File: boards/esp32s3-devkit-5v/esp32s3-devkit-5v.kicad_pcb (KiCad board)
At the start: 4 copper layers, 59.3 x 38 mm, 37 parts, among them J1 Conn_01x17_Pin, J2 Conn_01x17_Pin, J3 USB_C_Receptacle_USB2.0_16P, Q1 AO3401A, SW1 MK-12C03-G015, SW2 RESET, SW3 BOOT, U1 TPS63070RNMR, U2 ESP32-S3-WROOM-1-N16, U3 USBLC6-2SC6

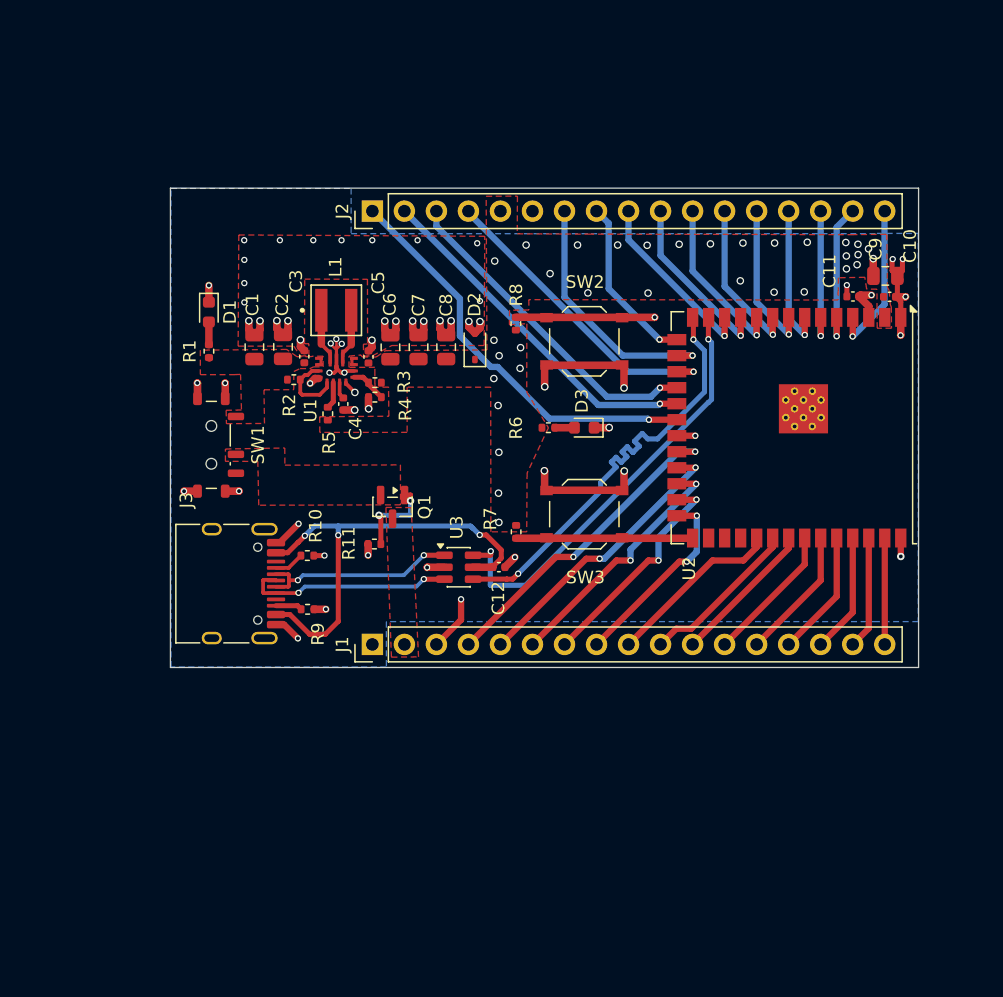
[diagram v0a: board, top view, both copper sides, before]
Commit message: feat(esp32s3-devkit-5v): add reviewed schematic and routed prototype
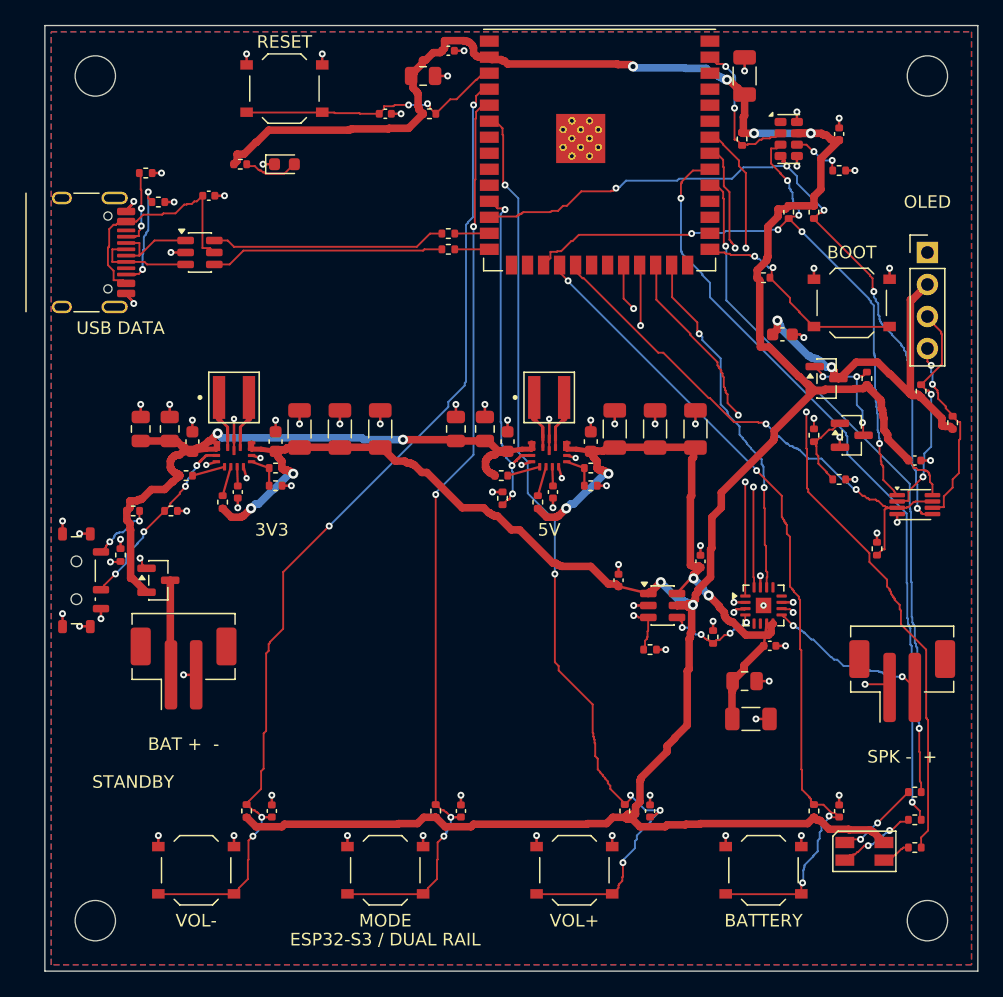
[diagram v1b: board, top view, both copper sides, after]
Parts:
- removed D3: LED, LED_SMD:LED_0603_1608Metric
- removed R2: 10kΩ, Resistor_SMD:R_0402_1005Metric
- added C13: 10µF, Capacitor_SMD:C_0603_1608Metric, F.Cu at (143.3, 103.0)
- added C14: 22µF, Capacitor_SMD:C_1206_3216Metric, F.Cu at (145.2, 102.0)
- added C15: 22µF, Capacitor_SMD:C_1206_3216Metric, F.Cu at (148.4, 102.0)
- added C16: 22µF, Capacitor_SMD:C_1206_3216Metric, F.Cu at (151.6, 102.0)
- added C17: 22µF, Capacitor_SMD:C_0805_2012Metric, F.Cu at (130.0, 74.0)
- added C18: 0.1µF, Capacitor_SMD:C_0402_1005Metric, F.Cu at (132.0, 72.0)
- added C19: 1µF, Capacitor_SMD:C_0402_1005Metric, F.Cu at (127.0, 77.0)
- added C20: 0.1µF, Capacitor_SMD:C_0402_1005Metric, F.Cu at (113.0, 83.5)
- added C21: 100µF, Capacitor_SMD:C_1206_3216Metric, F.Cu at (155.5, 74.0)
- added C22: 0.1µF, Capacitor_SMD:C_0402_1005Metric, F.Cu at (118.0, 132.3)
- added C23: 0.1µF, Capacitor_SMD:C_0402_1005Metric, F.Cu at (133.0, 132.3)
- added C24: 0.1µF, Capacitor_SMD:C_0402_1005Metric, F.Cu at (148.0, 132.3)
- added C25: 0.1µF, Capacitor_SMD:C_0402_1005Metric, F.Cu at (163.0, 132.3)
- added C26: 100µF, Capacitor_SMD:C_1206_3216Metric, F.Cu at (156.0, 125.0)
- added C27: 10µF, Capacitor_SMD:C_0805_2012Metric, F.Cu at (155.5, 122.0)
- added C28: 0.1µF, Capacitor_SMD:C_0402_1005Metric, F.Cu at (157.5, 119.2)
- added C29: 0.1µF, Capacitor_SMD:C_0402_1005Metric, F.Cu at (163.0, 78.6)
- added C30: 0.1µF, Capacitor_SMD:C_0402_1005Metric, F.Cu at (169.0, 104.5)
- added C31: 1µF, Capacitor_SMD:C_0603_1608Metric, F.Cu at (158.5, 94.5)
- added C32: 0.1µF, Capacitor_SMD:C_0402_1005Metric, F.Cu at (145.5, 114.0)
- added C33: 0.1µF, Capacitor_SMD:C_0402_1005Metric, F.Cu at (152.0, 112.5)
- added H1: M3, MountingHole_3.2mm_M3, F.Cu at (104.0, 74.0)
- added H2: M3, MountingHole_3.2mm_M3, F.Cu at (170.0, 74.0)
- added H3: M3, MountingHole_3.2mm_M3, F.Cu at (104.0, 141.0)
- added H4: M3, MountingHole_3.2mm_M3, F.Cu at (170.0, 141.0)
- added J4: Conn_01x04_Pin, Connector_PinHeader_2.54mm:PinHeader_1x04_P2.54mm_Vertical, F.Cu at (170.0, 88.0)
- added L2: 1.5µH, TPS63070:IND_XFL4020-152MEC, F.Cu at (140.0, 99.5)
- added Q2: AO3401A, Package_TO_SOT_SMD:SOT-23, F.Cu at (162.0, 98.0)
- added Q3: MMBT3904, Package_TO_SOT_SMD:SOT-23, F.Cu at (164.0, 102.5)
- added R12: 10kΩ, Resistor_SMD:R_0402_1005Metric, F.Cu at (157.0, 90.0)
- added R13: 10kΩ, Resistor_SMD:R_0402_1005Metric, F.Cu at (130.5, 77.0)
- added R14: 5.1kΩ, Resistor_SMD:R_0402_1005Metric, F.Cu at (109.0, 84.0)
- added R15: 5.1kΩ, Resistor_SMD:R_0402_1005Metric, F.Cu at (108.0, 81.7)
- added R16: 4.7kΩ, Resistor_SMD:R_0402_1005Metric, F.Cu at (159.0, 84.8)
- added R17: 4.7kΩ, Resistor_SMD:R_0402_1005Metric, F.Cu at (161.0, 84.8)
- added R18: 10kΩ, Resistor_SMD:R_0402_1005Metric, F.Cu at (155.3, 79.0)
- added R19: 100kΩ, Resistor_SMD:R_0402_1005Metric, F.Cu at (136.3, 107.5)
- added R20: 100kΩ, Resistor_SMD:R_0402_1005Metric, F.Cu at (153.0, 118.5)
- added R21: 100kΩ, Resistor_SMD:R_0402_1005Metric, F.Cu at (165.2, 98.0)
- added R22: 10kΩ, Resistor_SMD:R_0402_1005Metric, F.Cu at (161.0, 102.5)
- added R23: 100kΩ, Resistor_SMD:R_0402_1005Metric, F.Cu at (163.0, 106.0)
- added R24: 10kΩ, Resistor_SMD:R_0402_1005Metric, F.Cu at (116.0, 132.3)
- added R25: 10kΩ, Resistor_SMD:R_0402_1005Metric, F.Cu at (131.0, 132.3)
- added R26: 10kΩ, Resistor_SMD:R_0402_1005Metric, F.Cu at (146.0, 132.3)
- added R27: 10kΩ, Resistor_SMD:R_0402_1005Metric, F.Cu at (161.0, 132.3)
- added R28: 330Ω, Resistor_SMD:R_0402_1005Metric, F.Cu at (169.0, 130.8)
- added R29: 150Ω, Resistor_SMD:R_0402_1005Metric, F.Cu at (169.0, 133.0)
- added R30: 150Ω, Resistor_SMD:R_0402_1005Metric, F.Cu at (169.0, 135.2)
- added R31: 10kΩ, Resistor_SMD:R_0402_1005Metric, F.Cu at (107.0, 108.5)
- added R32: 100kΩ, Resistor_SMD:R_0402_1005Metric, F.Cu at (110.0, 108.5)
- added R33: 10kΩ, Resistor_SMD:R_0402_1005Metric, F.Cu at (163.0, 81.5)
- added R34: 22Ω, Resistor_SMD:R_0402_1005Metric, F.Cu at (132.0, 86.5)
- added R35: 22Ω, Resistor_SMD:R_0402_1005Metric, F.Cu at (132.0, 87.8)
- added R36: 100kΩ, Resistor_SMD:R_0402_1005Metric, F.Cu at (166.0, 111.5)
- added R37: 4.7kΩ, Resistor_SMD:R_0402_1005Metric, F.Cu at (169.5, 99.0)
- added R38: 4.7kΩ, Resistor_SMD:R_0402_1005Metric, F.Cu at (172.0, 101.5)
- added R39: 100kΩ, Resistor_SMD:R_0402_1005Metric, F.Cu at (148.0, 119.5)
- added SW4: VOL-, Button_Switch_SMD:SW_Push_1P1T_XKB_TS-1187A, F.Cu at (112.0, 137.0)
- added SW5: MODE, Button_Switch_SMD:SW_Push_1P1T_XKB_TS-1187A, F.Cu at (127.0, 137.0)
- added SW6: VOL+, Button_Switch_SMD:SW_Push_1P1T_XKB_TS-1187A, F.Cu at (142.0, 137.0)
- added SW7: BATTERY, Button_Switch_SMD:SW_Push_1P1T_XKB_TS-1187A, F.Cu at (157.0, 137.0)
- added U4: USBLC6-2SC6, Package_TO_SOT_SMD:SOT-23-6, F.Cu at (112.3, 88.0)
- added U5: RV-3028-C7, Package_SON:MicroCrystal_C7_SON-8_1.5x3.2mm_P0.9mm, F.Cu at (159.0, 79.0)
- added U6: MAX98357A, Package_DFN_QFN:TQFN-16-1EP_3x3mm_P0.5mm_EP1.23x1.23mm, F.Cu at (157.0, 116.0)
- added U7: SN74LVC2G66DCUR, Package_SO:VSSOP-8_2.3x2mm_P0.5mm, F.Cu at (169.0, 108.0)
- added U8: SN74LVC1T45DBVR, Package_TO_SOT_SMD:SOT-23-6, F.Cu at (149.0, 116.0)
- C10: value 0.1µF -> 10µF; footprint Capacitor_SMD:C_0402_1005Metric -> Capacitor_SMD:C_0805_2012Metric
- C11: value 1µF -> 10µF; footprint Capacitor_SMD:C_0402_1005Metric -> Capacitor_SMD:C_0603_1608Metric
- C3, C5: footprint Capacitor_SMD:C_0402_1005Metric -> Capacitor_SMD:C_0603_1608Metric
- C6, C7, C8: footprint Capacitor_SMD:C_0805_2012Metric -> Capacitor_SMD:C_1206_3216Metric
- C9: value 22µF -> 10µF
- D2: value 3.6v -> 150141M173100; footprint Diode_SMD:D_SOD-323 -> LED_SMD:LED_RGB_Wuerth-PLCC4_3.2x2.8mm_150141M173100
- J1: value Conn_01x17_Pin -> Conn_01x02_Pin; footprint Connector_PinHeader_2.54mm:PinHeader_1x17_P2.54mm_Vertical -> Connector_JST:JST_PH_B2B-PH-SM4-TB_1x02-1MP_P2.00mm_Vertical
- J2: value Conn_01x17_Pin -> USB_C_Receptacle_USB2.0_16P; footprint Connector_PinHeader_2.54mm:PinHeader_1x17_P2.54mm_Vertical -> Connector_USB:USB_C_Receptacle_HRO_TYPE-C-31-M-12
- J3: value USB_C_Receptacle_USB2.0_16P -> Conn_01x02_Pin; footprint Connector_USB:USB_C_Receptacle_HRO_TYPE-C-31-M-12 -> Connector_JST:JST_PH_B2B-PH-SM4-TB_1x02-1MP_P2.00mm_Vertical
- R1, R6: value 1kΩ -> 100kΩ
- R10: value 5.1kΩ -> 100kΩ
- R11: value 100kΩ -> 1kΩ
- R3: value 470kΩ -> 10kΩ
- R4: value 150kΩ -> 470kΩ
- R5: value 100kΩ -> 150kΩ
- R8: value 10kΩ -> 680kΩ
- R9: value 5.1kΩ -> 130kΩ
- U2: value ESP32-S3-WROOM-1-N16 -> TPS63070RNMR; footprint RF_Module:ESP32-S3-WROOM-1 -> TPS63070:TPS63070
- U3: value USBLC6-2SC6 -> ESP32-S3-WROOM-1-N16; footprint Package_TO_SOT_SMD:SOT-23-6 -> RF_Module:ESP32-S3-WROOM-1
- moved J3 54.3 mm to (168.0, 122.0), turned to 0 degrees
- moved D2 50.6 mm to (165.0, 135.5), turned to 0 degrees
- moved U3 38.1 mm to (144.0, 76.5)
- moved C9 36.2 mm to (132.6, 102.0), turned to 90 degrees
- moved C10 33.8 mm to (134.9, 102.0), turned to 90 degrees
- moved R11 32.0 mm to (115.5, 81.0), turned to 0 degrees
- moved SW2 31.1 mm to (119.0, 75.0), turned to 0 degrees
- moved C11 29.7 mm to (136.7, 103.0), turned to 90 degrees
- moved SW3 27.0 mm to (164.0, 92.0)
- moved R6 26.5 mm to (114.1, 107.8), turned to 90 degrees
- moved R9 24.5 mm to (143.3, 106.5)
- moved J2 23.8 mm to (102.4, 88.0), turned to -90 degrees
- moved U2 22.8 mm to (140.0, 105.0), turned to 0 degrees
- moved Q1 19.5 mm to (109.0, 114.0), turned to 0 degrees
- moved R10 18.8 mm to (139.1, 107.8), turned to 90 degrees
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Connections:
- C1 pad 1: /VBAT_SW -> /PFET
- C10 pad 1: /3v3 -> /PFET
- C11 pad 1: Net-(U2-EN) -> /PFET
- C12 pad 1: Net-(U3-VBUS) -> Net-(U2-VAUX)
- C2 pad 1: /VBAT_SW -> /PFET
- C3 pad 1: /VBAT_SW -> /PFET
- C9 pad 1: /3v3 -> /PFET
- D2 pad 2: GND -> Net-(D2-BK)
- J1 pad 1: GND -> /VBAT
- J1 pad 2: /VBAT -> GND
- R1 pad 1: /VBAT_SW -> Net-(Q1-G)
- R1 pad 2: Net-(D1-A) -> GND
- R10 pad 1: Net-(J3-CC1) -> /5v
- R10 pad 2: GND -> Net-(U2-PG)
- R11 pad 1: Net-(Q1-G) -> /3v3
- R11 pad 2: GND -> Net-(D1-A)
- R3 pad 1: /3v3 -> /PFET
- R3 pad 2: Net-(U1-FB) -> Net-(U1-PS_SYNC)
- R4 pad 1: Net-(U1-FB) -> /3v3
- R4 pad 2: GND -> Net-(U1-FB)
- R5 pad 1: /3v3 -> Net-(U1-FB)
- R5 pad 2: Net-(U1-PG) -> GND
- R6 pad 2: Net-(D3-A) -> Net-(U1-PG)
- R7 pad 1: /3v3 -> /PFET
- R7 pad 2: Net-(U2-IO0) -> Net-(U2-PS_SYNC)
- R8 pad 1: /3v3 -> /5v
- R8 pad 2: Net-(U2-EN) -> Net-(U2-FB)
- R9 pad 1: Net-(J3-CC2) -> Net-(U2-FB)
- SW1 pad 1: /VBAT_SW -> /SW_ON
- SW1 pad 2: /PFET -> /EN_3V3
- SW1 pad 3: unconnected-(SW1-C-Pad3) -> GND
- SW2 pad 2: Net-(U2-EN) -> Net-(U3-EN)
- SW3 pad 2: Net-(U2-IO0) -> Net-(U3-IO0)
- U1 pad 1: Net-(U1-EN) -> Net-(U1-PS_SYNC)
- U1 pad 12: /VBAT_SW -> /PFET
- U1 pad 13: /VBAT_SW -> /PFET
- U1 pad 14: Net-(U1-EN) -> /EN_3V3
- U2 pad 1: GND -> Net-(U2-PS_SYNC)
- U2 pad 10: /GPIO17 -> GND
- U2 pad 11: /GPIO18 -> Net-(U2-L1)
- U2 pad 12: /GPIO8 -> /PFET
- U2 pad 13: /D- -> /PFET
- U2 pad 14: /D+ -> /GPIO18
- U2 pad 15: /GPIO3 -> GND
- U2 pad 2: /3v3 -> Net-(U2-PG)
- U2 pad 3: Net-(U2-EN) -> Net-(U2-VAUX)
- U2 pad 4: /GPIO4 -> GND
- U2 pad 5: /GPIO5 -> Net-(U2-FB)
- U2 pad 6: /GPIO6 -> GND
- U2 pad 7: /GPIO7 -> /5v
- U2 pad 8: /GPIO15 -> /5v
- U2 pad 9: /GPIO16 -> Net-(U2-L2)
- U3 pad 1: Net-(J3-D--PadA7) -> GND
- U3 pad 2: GND -> /3v3
- U3 pad 3: Net-(J3-D+-PadA6) -> Net-(U3-EN)
- U3 pad 4: /D+ -> /GPIO4
- U3 pad 5: Net-(U3-VBUS) -> /GPIO5
- U3 pad 6: /D- -> /GPIO6
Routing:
- net /3v3: track 1.37 -> 255.2 mm, vias 33 -> 8
- net /GPIO4: track 12.5 -> 81.4 mm, vias 1 -> 4
- net /GPIO6: track 11.4 -> 79.2 mm, vias 1 -> 5
- net /GPIO5: track 11.9 -> 73.9 mm, vias 1 -> 4
- net /PFET: track 0.00 -> 55.9 mm, vias 0 -> 2
- net /5v: track 0.00 -> 53.7 mm, vias 0 -> 4
- net /GPIO40: track 11.6 -> 62.8 mm, vias 0 -> 2
- net /GPIO39: track 12.8 -> 61.2 mm, vias 0 -> 2
- net /GPIO8: track 14.5 -> 61.0 mm, vias 1 -> 5
- net /GPIO10: track 26.2 -> 67.7 mm, vias 1 -> 4
- net /GPIO38: track 14.1 -> 55.4 mm, vias 0 -> 2
- net Net-(U3-VBUS): track 36.3 -> 0.00 mm, vias 3 -> 0
- net /GPIO12: track 32.7 -> 0.00 mm, vias 1 -> 0
- net Net-(U2-EN): track 32.0 -> 0.00 mm, vias 2 -> 0
- net /OLED_3V3: track 0.00 -> 31.0 mm, vias 0 -> 2
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- added copper zone on In2.Cu, net GND
- removed copper zone on F.Cu, net /3v3
- removed copper zone on In2.Cu, net /3v3
- removed copper zone on F.Cu, net /PFET
- removed copper zone on F.Cu, net /VBAT
- removed copper zone on F.Cu, net /VBAT_SW
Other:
- board size 59.3 x 38 mm -> 74 x 75 mm
- board text added: "3V3"
- board text added: "5V"
- board text added: "BAT + -"
- board text added: "BATTERY"
- board text added: "BOOT"
- board text added: "ESP32-S3 / DUAL RAIL"
- board text added: "MODE"
- board text added: "OLED"
- board text added: "RESET"
- board text added: "SPK - +"
- board text added: "STANDBY"
- board text added: "USB DATA"
- board text added: "VOL+"
- board text added: "VOL-"

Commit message: Compact dual-rail PCB and add safe power monitoring
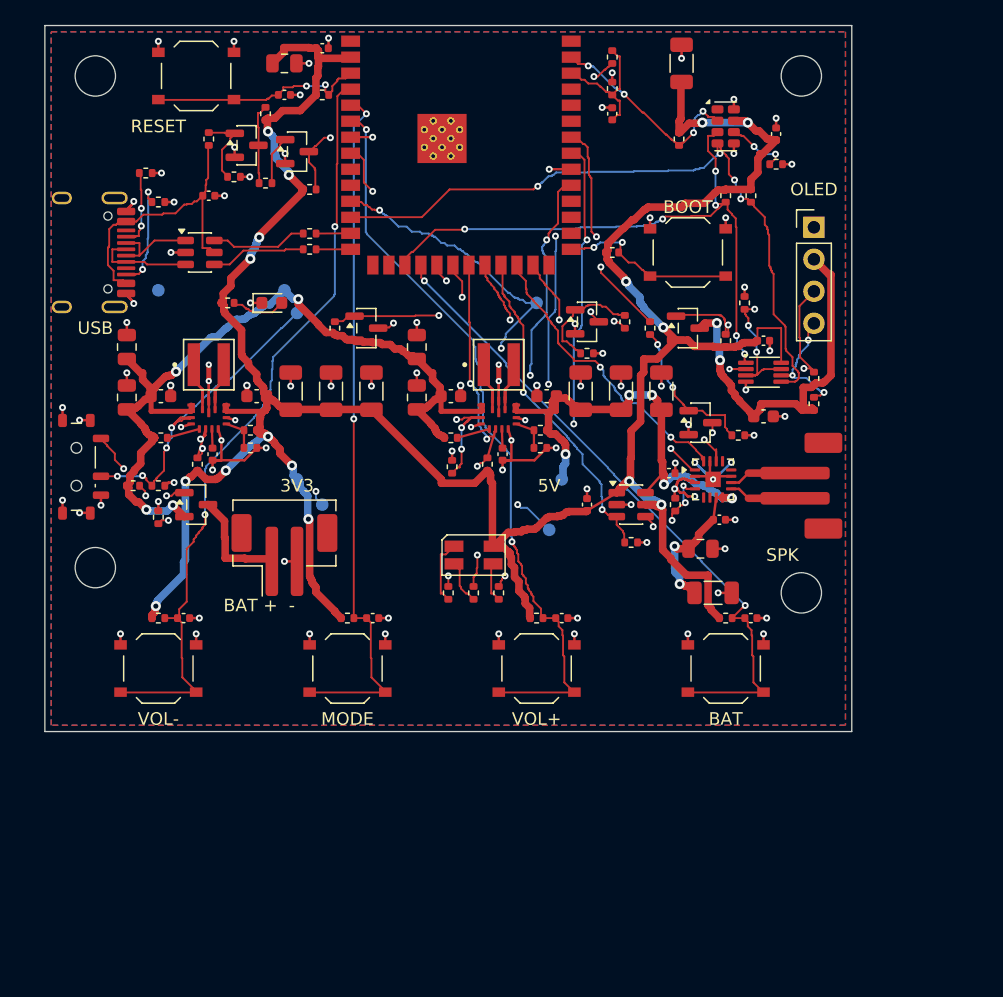
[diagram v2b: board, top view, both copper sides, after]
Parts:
- added C34: 0.1uF, Capacitor_SMD:C_0402_1005Metric, F.Cu at (145.0, 77.0)
- added Q4: MMBT3904, Package_TO_SOT_SMD:SOT-23, F.Cu at (116.0, 79.5)
- added Q5: MMBT3904, Package_TO_SOT_SMD:SOT-23, F.Cu at (120.0, 80.0)
- added Q6: AO3401A, Package_TO_SOT_SMD:SOT-23, F.Cu at (125.5, 94.0)
- added Q7: MMBT3904, Package_TO_SOT_SMD:SOT-23, F.Cu at (143.0, 93.5)
- added R40: 100k, Resistor_SMD:R_0402_1005Metric, F.Cu at (113.0, 79.0)
- added R41: 1M, Resistor_SMD:R_0402_1005Metric, F.Cu at (115.0, 82.0)
- added R42: 47k, Resistor_SMD:R_0402_1005Metric, F.Cu at (117.5, 77.0)
- added R43: 10k, Resistor_SMD:R_0402_1005Metric, F.Cu at (117.5, 82.5)
- added R44: 47k, Resistor_SMD:R_0402_1005Metric, F.Cu at (121.0, 83.0)
- added R45: 100k, Resistor_SMD:R_0402_1005Metric, F.Cu at (123.0, 94.0)
- added R46: 10k, Resistor_SMD:R_0402_1005Metric, F.Cu at (146.0, 93.5)
- added R47: 100k, Resistor_SMD:R_0402_1005Metric, F.Cu at (143.0, 96.0)
- added R48: 33k, Resistor_SMD:R_0402_1005Metric, F.Cu at (145.0, 72.5)
- added R49: 10k, Resistor_SMD:R_0402_1005Metric, F.Cu at (145.0, 75.0)
- added TP1: GND, TestPoint_Pad_D1.0mm, B.Cu at (109.0, 91.0)
- added TP2: PFET, TestPoint_Pad_D1.0mm, B.Cu at (119.0, 91.0)
- added TP3: 3v3, TestPoint_Pad_D1.0mm, B.Cu at (120.0, 106.0)
- added TP4: 5v, TestPoint_Pad_D1.0mm, B.Cu at (141.0, 106.0)
- added TP5: GPIO15, TestPoint_Pad_D1.0mm, B.Cu at (122.0, 108.0)
- added TP6: GPIO13, TestPoint_Pad_D1.0mm, B.Cu at (140.0, 110.0)
- added TP7: EN_3V3, TestPoint_Pad_D1.0mm, B.Cu at (120.0, 92.8)
- added TP8: GPIO18, TestPoint_Pad_D1.0mm, B.Cu at (139.0, 92.0)
- J2: footprint Connector_USB:USB_C_Receptacle_HRO_TYPE-C-31-M-12 -> Board:USB_C_HRO_Overhang
- J3: footprint Connector_JST:JST_PH_B2B-PH-SM4-TB_1x02-1MP_P2.00mm_Vertical -> Board:JST_PH_Speaker_Overhang
- SW1: value MK-12C03-G015 -> MSK12C02
- U3: footprint RF_Module:ESP32-S3-WROOM-1 -> Board:ESP32-S3-WROOM-1_Overhang
- moved R28 40.2 mm to (132.0, 115.0), turned to 90 degrees
- moved R29 39.4 mm to (134.0, 115.0), turned to 90 degrees
- moved D2 38.9 mm to (134.0, 112.0)
- moved R30 38.7 mm to (136.0, 115.0), turned to 90 degrees
- moved H3 28.0 mm to (104.0, 113.0)
- moved H4 27.9 mm to (160.0, 115.0)
- moved R36 22.1 mm to (155.5, 92.0)
- moved J3 17.4 mm to (160.0, 106.5), turned to -90 degrees
- moved C22 16.8 mm to (111.0, 117.0), turned to 0 degrees
- moved C23 16.8 mm to (126.0, 117.0), turned to 0 degrees
- moved C24 16.8 mm to (141.0, 117.0), turned to 0 degrees
- moved C25 16.8 mm to (156.0, 117.0), turned to 0 degrees
- moved R24 16.8 mm to (109.0, 117.0), turned to 0 degrees
- moved R25 16.8 mm to (124.0, 117.0), turned to 0 degrees
- moved R26 16.8 mm to (139.0, 117.0), turned to 0 degrees
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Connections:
- R10 pad 1: /5v -> /3v3
- R10 pad 2: Net-(U2-PG) -> /GPIO13
- R6 pad 2: Net-(U1-PG) -> /GPIO15
- U1 pad 2: Net-(U1-PG) -> /GPIO15
- U2 pad 2: Net-(U2-PG) -> /GPIO13
- U3 pad 20: unconnected-(U3-IO12-Pad20) -> /GPIO12
- U3 pad 21: unconnected-(U3-IO13-Pad21) -> /GPIO13
- U3 pad 38: unconnected-(U3-IO2-Pad38) -> /GPIO2
- U3 pad 7: unconnected-(U3-IO7-Pad7) -> /GPIO7
- U3 pad 8: unconnected-(U3-IO15-Pad8) -> /GPIO15
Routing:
- net /GPIO15: track 0.00 -> 45.4 mm, vias 0 -> 4
- net GND: track 82.9 -> 114.1 mm, vias 85 -> 93
- net /Power monitoring/BAT_MEAS: track 0.00 -> 29.4 mm, vias 0 -> 2
- net /3v3: track 255.2 -> 227.0 mm, vias 8 -> 16
- net /GPIO13: track 0.00 -> 27.0 mm, vias 0 -> 4
- net /GPIO40: track 62.8 -> 38.1 mm, vias 2 -> 3
- net Net-(Q6-G): track 0.00 -> 21.7 mm, vias 0 -> 2
- net /GPIO39: track 61.2 -> 39.6 mm, vias 2 -> 4
- net /GPIO4: track 81.4 -> 61.6 mm, vias 4 -> 2
- net /GPIO6: track 79.2 -> 59.8 mm, vias 5 -> 2
- net /GPIO38: track 55.4 -> 36.5 mm, vias 2 -> 3
- net /GPIO5: track 73.9 -> 55.6 mm, vias 4 -> 2
- net /GPIO12: track 0.00 -> 16.8 mm, vias 0 -> 2
- net /GPIO10: track 67.7 -> 53.0 mm, vias 4 -> 2
- net /EN_3V3: track 16.8 -> 29.2 mm
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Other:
- board size 74 x 75 mm -> 64 x 56 mm
- board text added: "BAT"
- board text added: "SPK"
- board text added: "USB"
- board text removed: "BATTERY"
- board text removed: "ESP32-S3 / DUAL RAIL"
- board text removed: "SPK - +"
- board text removed: "STANDBY"
- board text removed: "USB DATA"
